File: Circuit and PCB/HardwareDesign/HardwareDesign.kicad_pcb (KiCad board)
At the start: 2 copper layers, 91.5 x 49.6 mm, 27 parts, among them P1 282837-2, SW1 SW_MEC_5E, U1 AMS1117-3.3, U2 ESP32-WROOM-32D, U3 LM2596S-5, U4 LCD-16X2

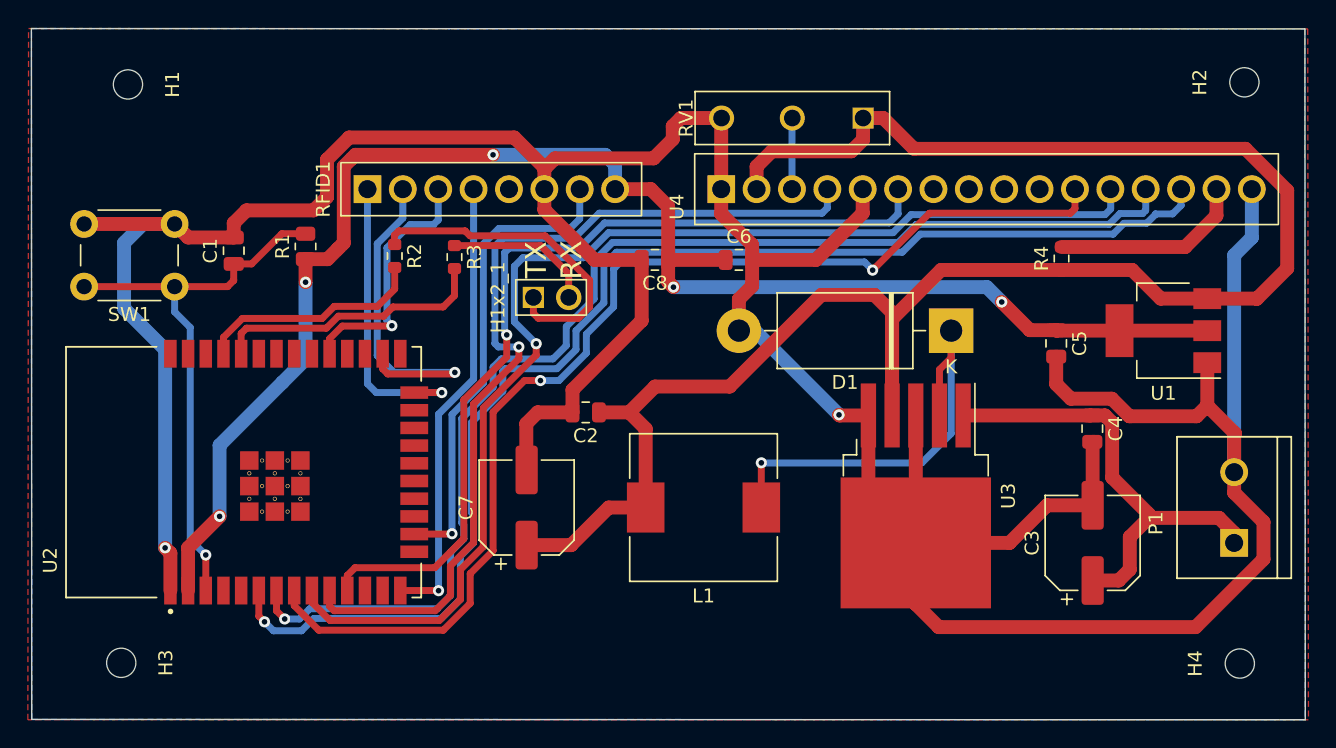
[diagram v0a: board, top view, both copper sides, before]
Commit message: add USB-C connector
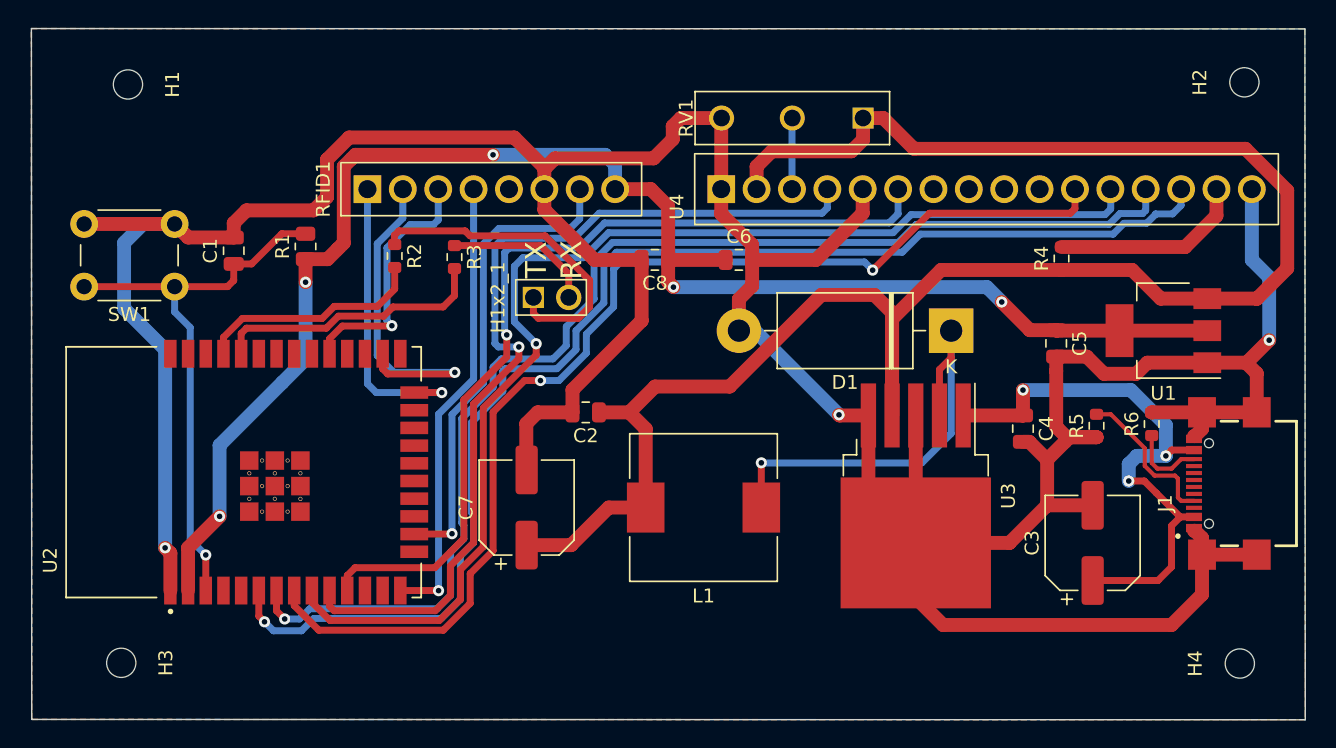
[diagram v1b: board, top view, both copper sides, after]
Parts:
- removed P1: 282837-2, Terminal Block:TE_282837-2
- added J1: USB4110-GF-A_REVB, USB-C:GCT_USB4110-GF-A_REVB, F.Cu at (203.9, 107.5)
- added R5: 5.1k, Resistor_SMD:R_0603_1608Metric, F.Cu at (195.9, 103.4)
- added R6: 5.1k, Resistor_SMD:R_0603_1608Metric, F.Cu at (199.8, 103.2)
- moved C4 4.98 mm to (190.6, 103.6)
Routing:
- net Net-(J1-PadA5): track 0.00 -> 11.1 mm
- net VCC: track 33.3 -> 41.6 mm, vias 0 -> 3
- net GND: track 277.1 -> 284.1 mm, vias 2 -> 3
- net Net-(J1-PadB5): track 0.00 -> 5.46 mm
